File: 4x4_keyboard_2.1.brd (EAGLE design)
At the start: 69.5 x 145.2 mm, 77 parts, among them U2 AMS1117-5.0

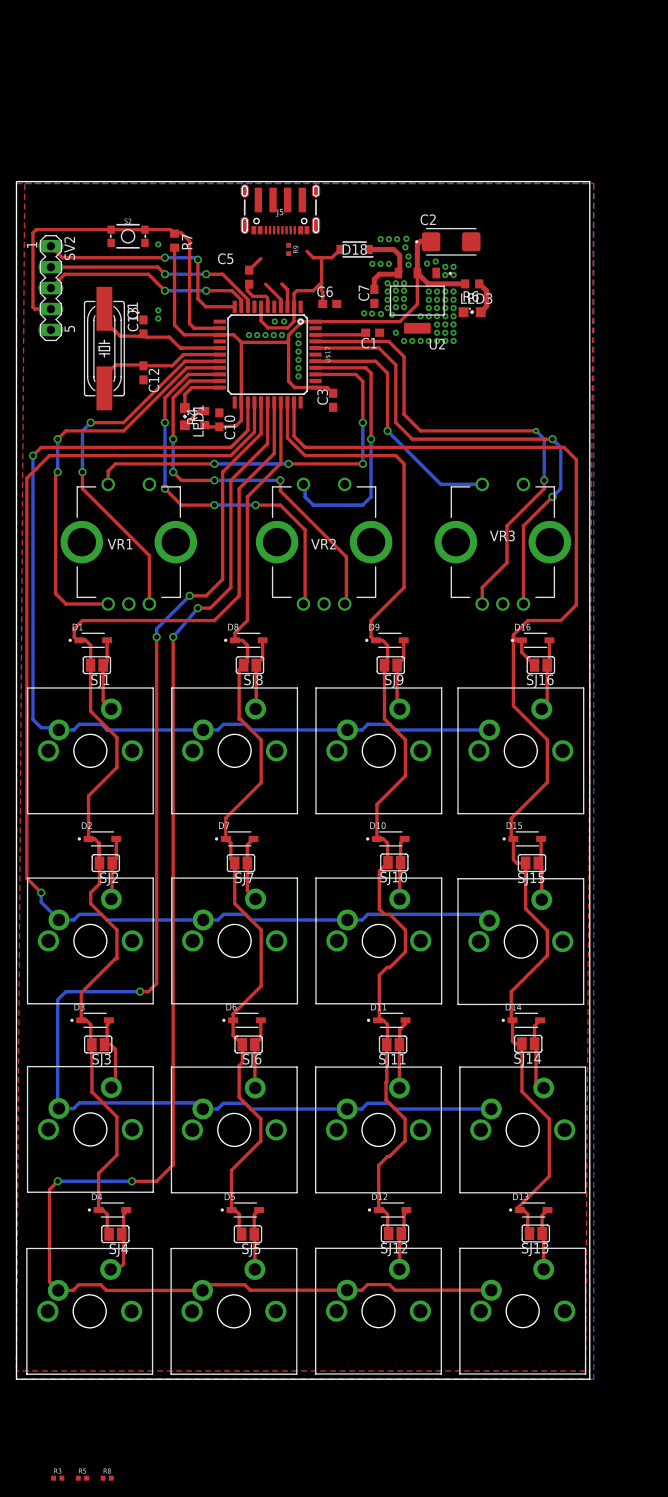
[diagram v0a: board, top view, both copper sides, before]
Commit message: USB C is connect and final output without error
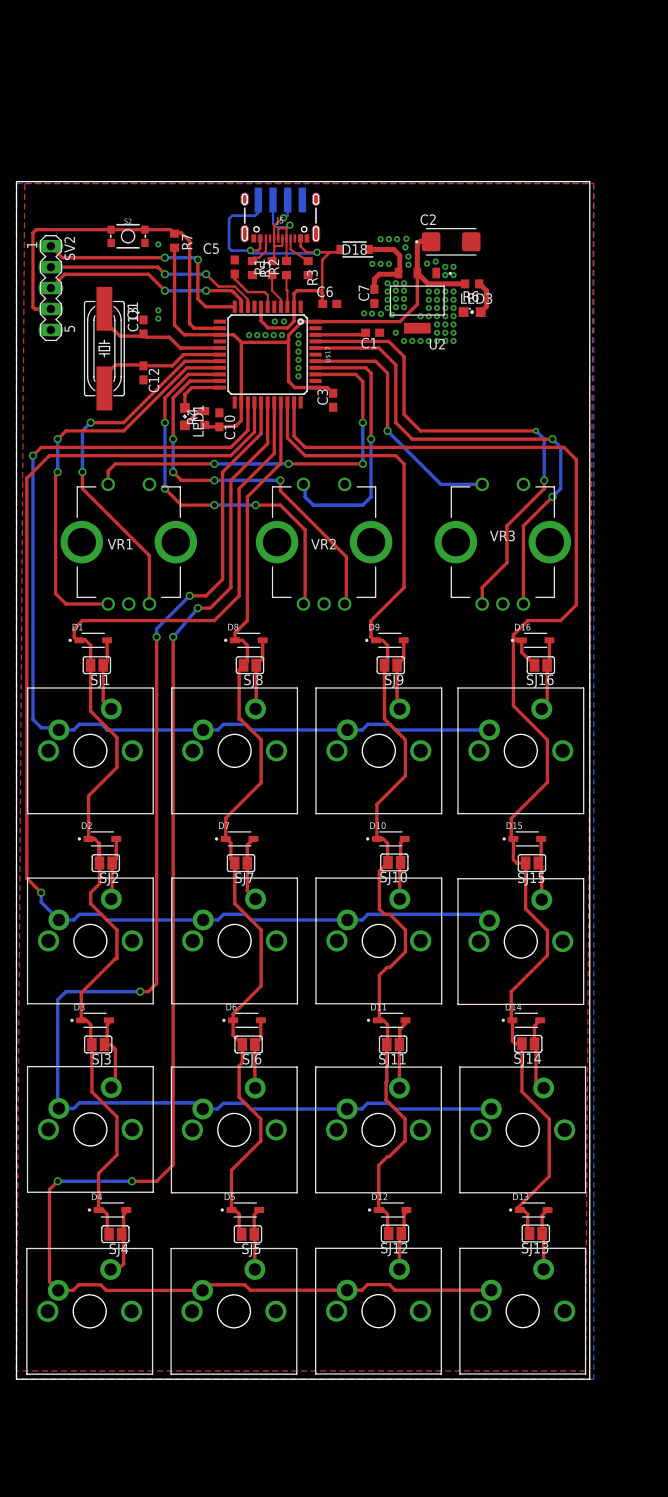
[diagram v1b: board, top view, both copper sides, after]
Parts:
- removed R8, R9: 5.1k, SparkFun-Resistors:0402-TIGHT
- added R1, R2: 5.1k, audio amplifier example:R0603
- R3, R5: device SparkFun-Resistors:0402-TIGHT -> audio amplifier example:R0603
- moved R3 149.9 mm to (35.4, 134.7), turned to 270 degrees
- moved R5 148.2 mm to (28.6, 134.7), turned to 270 degrees
- moved C5 2.14 mm to (26.5, 134.9)
- moved J5 1.00 mm to (32.0, 138.0)
- flipped JP14 to the bottom
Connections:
- net D+: now also R1.1; no longer R9.2
- net D-: now also R2.1; no longer R8.2
- net D-_HV: now also R2.2; no longer R8.1
- net DP_HV: now also R1.2; no longer R9.1
- net GND: now also R3.2, R5.2; no longer R3.1, R5.1
- net N$13: now also R5.1; no longer R3.2
- net N$7: now also R3.1; no longer R5.2
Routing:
- net V_USB: track 24.1 -> 48.8 mm, vias 0 -> 2
- net D-_HV: track 0.00 -> 11.9 mm, vias 0 -> 1
- net DP_HV: track 0.00 -> 10.3 mm, vias 0 -> 1
- net N$7: track 0.00 -> 3.89 mm
- net N$13: track 0.00 -> 3.78 mm
- net UCAP: track 4.75 -> 6.84 mm
- net GND: track 2.00 -> 0.00 mm
- net D-: track 3.07 -> 3.89 mm
- net D+: track 3.51 -> 4.29 mm

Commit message: change location of cherry switches
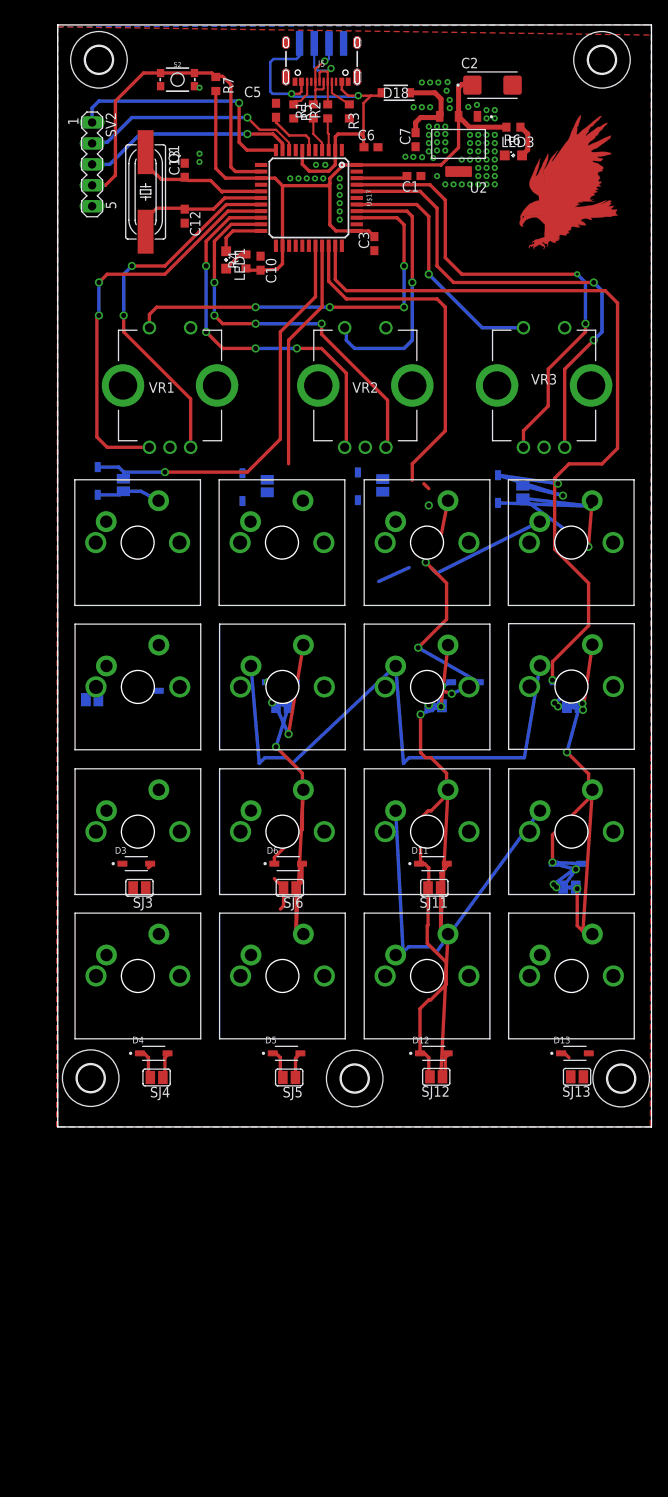
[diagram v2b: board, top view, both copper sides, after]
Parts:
- added H1, H2, H4, H5, H6: MOUNT-HOLE3.3, holes:3,3
- added U$19: (no value), logo:EAGLE-TOP-12MM
- moved U$14 41.1 mm to (32.2, 48.9)
- moved U$13 41.1 mm to (14.7, 48.9)
- moved U$16 41.1 mm to (67.3, 48.9)
- moved U$15 41.1 mm to (49.8, 48.9)
- moved U$12 36.6 mm to (67.3, 66.4)
- moved U$11 36.6 mm to (49.8, 66.4)
- moved U$10 36.6 mm to (32.2, 66.4)
- moved U$9 36.6 mm to (14.7, 66.4)
- moved U$8 31.5 mm to (67.3, 84.0)
- moved U$7 31.4 mm to (49.8, 84.0)
- moved U$6 31.3 mm to (32.2, 84.0)
- moved U$5 31.3 mm to (14.7, 84.0)
- moved U$4 26.0 mm to (67.3, 101.5)
- moved U$3 25.9 mm to (49.8, 101.5)
- moved U$2 25.9 mm to (32.2, 101.5)
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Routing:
- net ROW4: track 181.0 -> 0.00 mm, vias 4 -> 0
- net ROW3: track 157.1 -> 43.1 mm, vias 3 -> 0
- net ROW1: track 120.3 -> 19.0 mm, vias 1 -> 0
- net COL1: track 135.5 -> 53.9 mm, vias 0 -> 1
- net ROW2: track 142.6 -> 71.7 mm, vias 1 -> 0
- net COL2: track 114.9 -> 66.2 mm, vias 0 -> 3
- net N$8: track 8.71 -> 35.0 mm, vias 0 -> 2
- net N$12: track 9.09 -> 29.8 mm, vias 0 -> 2
- net N$9: track 8.52 -> 25.7 mm
- net N$22: track 8.52 -> 25.6 mm
- net N$15: track 7.54 -> 21.0 mm
- net N$23: track 8.01 -> 20.0 mm, vias 0 -> 2
- net N$25: track 8.68 -> 0.00 mm
- net N$18: track 9.56 -> 1.07 mm
- net N$10: track 7.69 -> 16.1 mm, vias 0 -> 2
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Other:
- board size 69.5 x 145.2 mm -> 72 x 133.6 mm

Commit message: routing cherry mx switch and correct the position of diode and rotary encoder
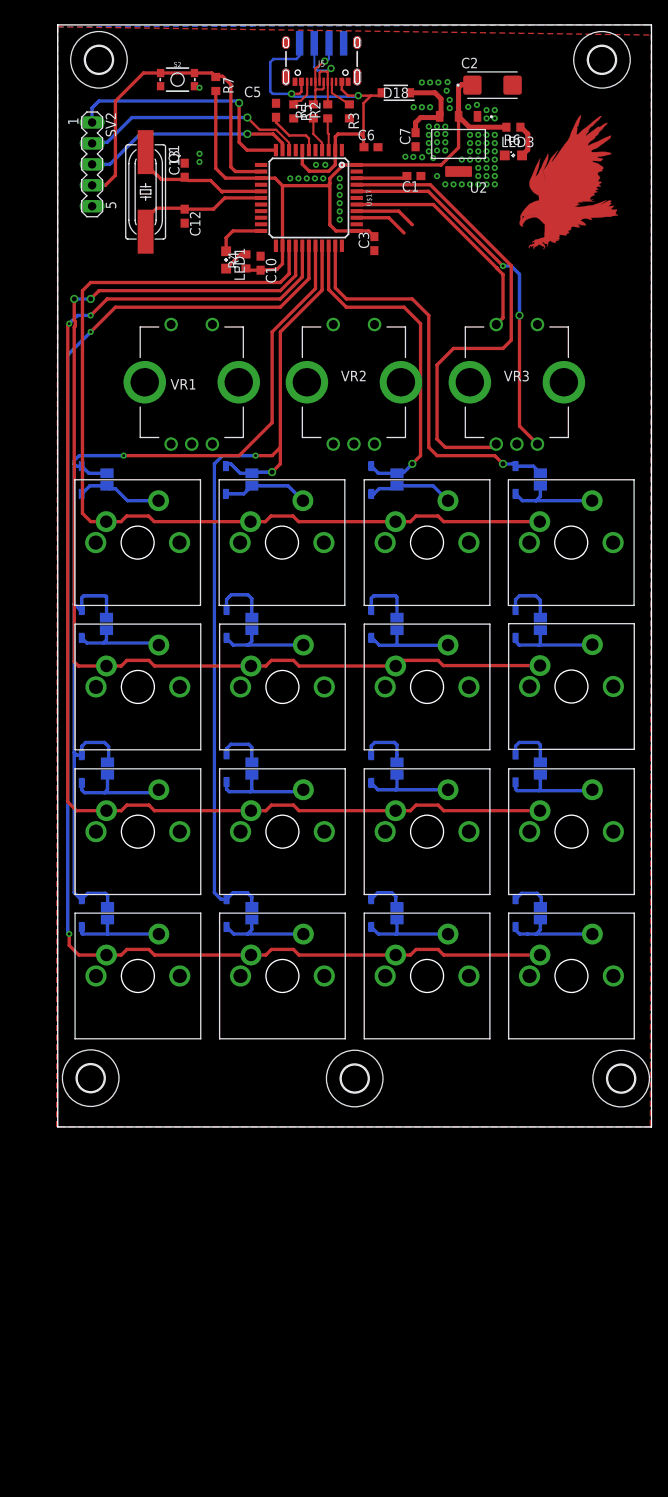
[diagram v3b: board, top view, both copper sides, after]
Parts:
- moved SJ4 20.8 mm to (11.0, 56.5), flipped to the bottom, turned to 90 degrees
- moved SJ5 20.4 mm to (28.5, 56.5), flipped to the bottom, turned to 90 degrees
- moved SJ12 20.4 mm to (46.1, 56.5), flipped to the bottom, turned to 90 degrees
- moved SJ13 20.3 mm to (63.5, 56.5), flipped to the bottom, turned to 90 degrees
- moved D4 19.1 mm to (7.92, 56.5), flipped to the bottom, turned to 270 degrees
- moved D12 18.6 mm to (43.0, 56.5), flipped to the bottom, turned to 270 degrees
- moved D5 18.5 mm to (25.5, 56.5), flipped to the bottom, turned to 270 degrees
- moved D13 18.5 mm to (60.5, 56.5), flipped to the bottom, turned to 270 degrees
- moved SJ6 15.2 mm to (28.5, 74.0), flipped to the bottom, turned to 90 degrees
- moved SJ11 15.1 mm to (46.1, 74.0), flipped to the bottom, turned to 90 degrees
- moved SJ3 15.0 mm to (11.0, 74.0), flipped to the bottom, turned to 90 degrees
- moved SJ14 14.8 mm to (63.5, 74.0), turned to 90 degrees
- moved D6 13.8 mm to (25.5, 74.1), flipped to the bottom, turned to 270 degrees
- moved D11 13.7 mm to (43.0, 74.0), flipped to the bottom, turned to 270 degrees
- moved D10 13.4 mm to (43.0, 91.6), turned to 270 degrees
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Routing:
- net ROW4: track 0.00 -> 168.1 mm, vias 0 -> 2
- net ROW3: track 43.1 -> 151.9 mm, vias 0 -> 2
- net ROW1: track 19.0 -> 113.9 mm
- net COL4: track 160.5 -> 66.7 mm, vias 9 -> 1
- net COL1: track 53.9 -> 128.9 mm
- net COL3: track 130.6 -> 60.1 mm, vias 7 -> 1
- net ROW2: track 71.7 -> 134.1 mm, vias 0 -> 2
- net COL2: track 66.2 -> 116.7 mm, vias 3 -> 2
- net A1: track 49.0 -> 0.00 mm, vias 2 -> 0
- net B2: track 47.3 -> 0.00 mm, vias 4 -> 0
- net A2: track 47.0 -> 0.00 mm, vias 4 -> 0
- net B1: track 44.5 -> 0.00 mm, vias 2 -> 0
- net SW1: track 48.9 -> 6.51 mm, vias 4 -> 0
- net SW2: track 32.4 -> 7.42 mm, vias 1 -> 0
- net N$8: track 35.0 -> 11.7 mm, vias 2 -> 0
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
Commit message: make position uniform
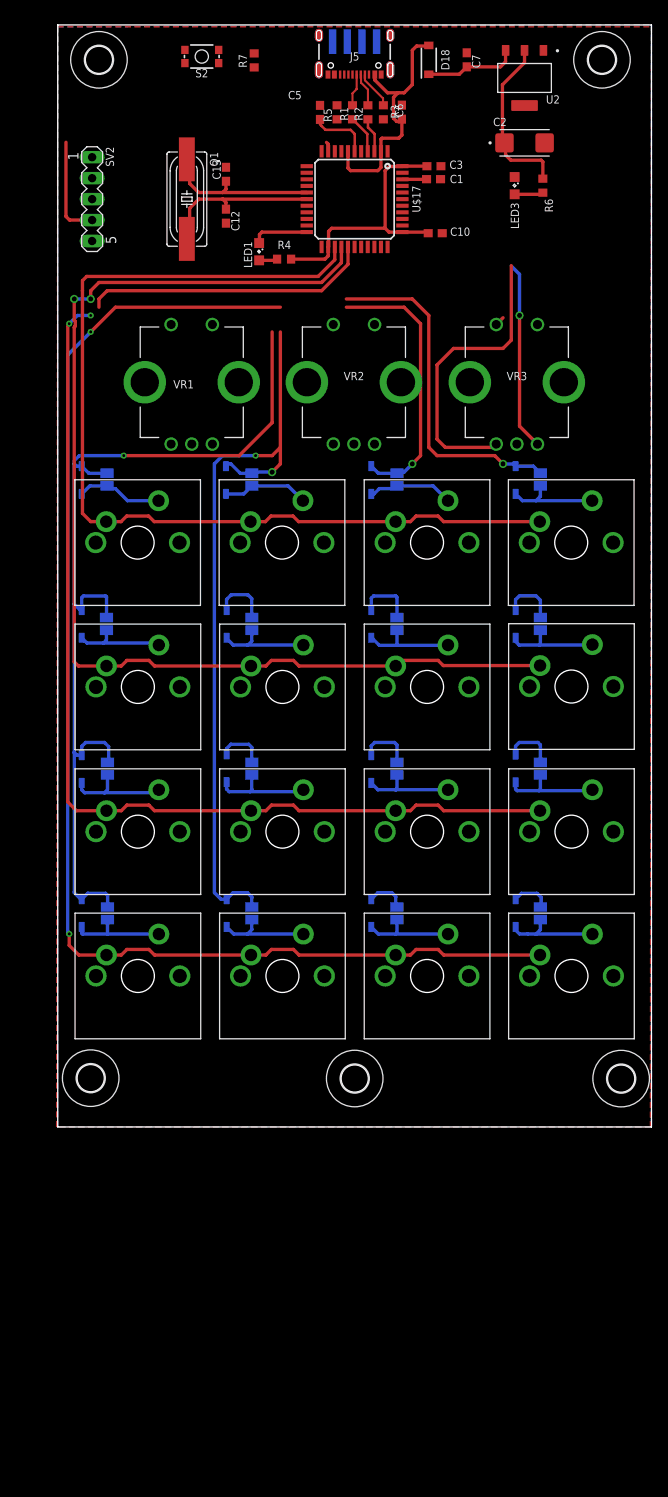
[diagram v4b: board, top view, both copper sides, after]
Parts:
- removed U$19: (no value), logo:EAGLE-TOP-12MM
- moved C10 21.5 mm to (50.8, 139.0), turned to 180 degrees
- moved C3 11.8 mm to (50.6, 147.1), turned to 180 degrees
- moved C7 11.5 mm to (54.6, 160.0), turned to 270 degrees
- moved U2 11.3 mm to (61.6, 157.8)
- moved C2 8.01 mm to (61.6, 149.9)
- moved R6 7.94 mm to (63.8, 144.7), turned to 90 degrees
- moved C6 5.67 mm to (46.7, 153.7), turned to 270 degrees
- moved D18 5.66 mm to (50.0, 160.0), turned to 90 degrees
- moved U$17 5.54 mm to (41.0, 143.1)
- moved R7 5.47 mm to (28.8, 159.9), turned to 90 degrees
- moved C5 5.34 mm to (36.8, 153.6)
- moved R5 5.26 mm to (38.9, 153.6)
- moved Q1 5.08 mm to (20.7, 143.1)
- moved C13 5.02 mm to (25.4, 146.1)
- moved C12 5.00 mm to (25.4, 141.0)
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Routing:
- net RESET: track 42.3 -> 12.3 mm
- net MISO: track 29.7 -> 0.00 mm, vias 1 -> 0
- net VCC: track 82.7 -> 53.3 mm
- net SCK: track 27.3 -> 0.00 mm, vias 1 -> 0
- net SW3: track 27.7 -> 1.16 mm
- net MOSI: track 25.9 -> 1.17 mm, vias 1 -> 0
- net A3: track 58.8 -> 36.0 mm
- net B3: track 45.4 -> 22.9 mm, vias 2 -> 1
- net V_USB: track 48.8 -> 31.7 mm, vias 2 -> 0
- net COL1: track 128.9 -> 116.3 mm
- net COL2: track 116.7 -> 104.1 mm
- net ROW4: track 168.1 -> 159.2 mm
- net COL3: track 60.1 -> 51.8 mm
- net D-_HV: track 11.9 -> 4.09 mm, vias 1 -> 0
- net SW2: track 7.42 -> 0.00 mm
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
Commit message: Routing is almost complete with error
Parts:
- moved C10 1.96 mm to (49.0, 138.2), turned to 90 degrees
- moved LED1 1.15 mm to (30.6, 136.9)
- moved R4 1.14 mm to (33.6, 135.8)
- moved S2 0.96 mm to (21.5, 160.6), turned to 0 degrees
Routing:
- net COL3: track 51.8 -> 119.2 mm
- net COL4: track 59.7 -> 115.7 mm
- net SW1: track 0.00 -> 55.9 mm, vias 0 -> 4
- net RESET: track 12.3 -> 65.2 mm
- net A2: track 0.00 -> 44.8 mm, vias 0 -> 1
- net B2: track 0.00 -> 44.1 mm, vias 0 -> 1
- net VCC: track 53.3 -> 97.1 mm
- net SCK: track 0.00 -> 41.8 mm, vias 0 -> 2
- net B1: track 0.00 -> 40.5 mm, vias 0 -> 1
- net A1: track 0.00 -> 39.9 mm, vias 0 -> 1
- net MOSI: track 1.17 -> 38.2 mm, vias 0 -> 2
- net MISO: track 0.00 -> 36.4 mm, vias 0 -> 2
- net SW2: track 0.00 -> 33.3 mm, vias 0 -> 2
- net SW3: track 1.16 -> 24.4 mm
- net B3: track 22.9 -> 43.3 mm, vias 1 -> 0
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
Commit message: Routing complete
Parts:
- moved H4 1.33 mm to (72.0, 36.5)
- moved R3 1.14 mm to (45.6, 153.6)
- moved C6 1.00 mm to (47.7, 153.6)
- moved H1 1.00 mm to (72.0, 160.0)
- moved H5 1.00 mm to (10.0, 36.5)
- moved R2 0.64 mm to (43.3, 153.6)
- moved C5 0.38 mm to (36.4, 153.6)
- moved R1 0.13 mm to (40.9, 153.6)
- moved R5 0.13 mm to (38.7, 153.6)
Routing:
- net GND: track 0.00 -> 9.35 mm
- net D-_HV: track 13.6 -> 14.2 mm
- net N$7: track 4.66 -> 5.25 mm
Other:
- board size 72 x 133.6 mm -> 72 x 134.4 mm
